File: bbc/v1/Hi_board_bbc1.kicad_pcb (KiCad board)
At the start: 2 copper layers, 55 x 61.1 mm, 15 parts, among them J1 sw-latch, J2 led-latch, J3 GLVMP, SW1 BSPD_RESET, SW2 IMD_RESET, SW3 BMS_RESET

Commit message: Add files via upload
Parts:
- moved J3 7.64 mm to (141.2, 112.3)
- moved J2 7.20 mm to (130.7, 108.5)
- moved R6 6.91 mm to (161.0, 122.4)
- moved R1 6.76 mm to (120.6, 122.4)
- moved J1 6.69 mm to (157.5, 108.4)
- moved D3 6.37 mm to (154.4, 127.5)
- moved D1 6.25 mm to (124.7, 127.5)
- moved R5 5.95 mm to (150.4, 132.6)
- moved R2 5.86 mm to (131.3, 132.6)
- moved R3 5.68 mm to (135.6, 122.4)
- moved R4 5.68 mm to (146.3, 132.6)
- moved D2 5.59 mm to (139.7, 127.5)
- moved SW3 3.24 mm to (153.7, 146.5)
- moved SW1 3.10 mm to (123.7, 146.0)
- moved SW2 2.22 mm to (138.5, 146.0)
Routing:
- net +12V: track 111.4 -> 86.3 mm
- net 0: track 86.6 -> 76.6 mm
- net BMS_RESET: track 52.3 -> 45.7 mm
- net BMS_LED: track 51.0 -> 44.6 mm
- net IMD_LED: track 42.3 -> 38.5 mm
- net BSPD_RESET: track 80.6 -> 76.9 mm
- net IMD_RESET: track 50.3 -> 48.0 mm
- net Net-(R5-Pad1): track 12.7 -> 10.7 mm
- net Net-(R3-Pad1): track 12.7 -> 10.7 mm
- net BSPD_LED: track 22.3 -> 20.3 mm
- net Net-(D3-A): track 11.1 -> 9.58 mm
- net Net-(D1-A): track 10.1 -> 9.16 mm
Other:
- board size 55 x 61.1 mm -> 47.8 x 50.3 mm

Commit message: Add files via upload
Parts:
- moved SW3 0.72 mm to (153.2, 146.0)
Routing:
- net BMS_RESET: track 45.7 -> 44.4 mm
- net +12V: track 86.3 -> 86.9 mm
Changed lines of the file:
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@@
 	(footprint "Button_Switch_THT:SW_PUSH_6mm"
 		(layer "F.Cu")
-		(at 153.706 146.506 90)
+		(at 153.198 145.998 90)
 		(descr "Generic 6mm SW tactile push button")
 		(tags "tact sw push 6mm")
@@
 			(keep_text_aligned yes)
 		)
-		(gr_text "1.36"
+		(gr_text "34.544"
 			(at 178.174 118.872 90)
 			(layer "Cmts.User")
@@
 			(keep_text_aligned yes)
 		)
-		(gr_text "0.755"
+		(gr_text "19.178"
 			(at 166.998 111.189 90)
 			(layer "Cmts.User")
@@
 			(keep_text_aligned yes)
 		)
-		(gr_text "1.16"
+		(gr_text "29.464"
 			(at 140.716 99.434 0)
 			(layer "Cmts.User")
@@
 		(layer "Cmts.User")
 		(pts
+			(xy 140.716 142.748) (xy 155.448 142.748)
+		)
+		(height 13.252)
+		(orientation 0)
+		(format
+			(prefix "")
+			(suffix "")
+			(units 3)
+			(units_format 0)
+			(precision 4)
+			(suppress_zeroes yes)
+		)
+		(style
+			(thickness 0.1)
+			(arrow_length 1.27)
+			(text_position_mode 0)
+			(arrow_direction outward)
+			(extension_height 0.58642)
+			(extension_offset 0.5)
+			(keep_text_aligned yes)
+		)
+		(gr_text "14.732"
+			(at 148.082 154.85 0)
+			(layer "Cmts.User")
+			(effects
+				(font
+					(size 1 1)
+					(thickness 0.15)
+				)
+			)
+		)
+	)
+	(dimension
+		(type orthogonal)
+		(layer "Cmts.User")
+		(pts
 			(xy 155.448 120.778) (xy 164.592 104.14)
 		)
@@
 			(keep_text_aligned yes)
 		)
-		(gr_text "0.36"
+		(gr_text "9.144"
 			(at 160.02 99.434 0)
 			(layer "Cmts.User")
@@
 			(keep_text_aligned yes)
 		)
-		(gr_text "1.88"
+		(gr_text "47.752"
 			(at 140.716 92.322 0)
 			(layer "Cmts.User")
@@
 		)
 	)
+	(dimension
+		(type orthogonal)
+		(layer "Cmts.User")
+		(pts
+			(xy 125.984 142.748) (xy 140.716 142.748)
+		)
+		(height 13.252)
+		(orientation 0)
+		(format
+			(prefix "")
+			(suffix "")
+			(units 3)
+			(units_format 0)
+			(precision 4)
+			(suppress_zeroes yes)
+		)
+		(style
+			(thickness 0.1)
+			(arrow_length 1.27)
+			(text_position_mode 0)
+			(arrow_direction outward)
+			(extension_height 0.58642)
+			(extension_offset 0.5)
+			(keep_text_aligned yes)
+		)
+		(gr_text "14.732"
+			(at 133.35 154.85 0)
+			(layer "Cmts.User")
+			(effects
+				(font
+					(size 1 1)
+					(thickness 0.15)
+				)
+			)
+		)
+	)
 	(segment
 		(start 127.249 128.275)
@@
 	)
 	(segment
-		(start 158.076 146.506)
-		(end 158.206 146.506)
+		(start 125.476 135.128)
+		(end 125.476 138.176)
 		(width 0.8)
-		(layer "F.Cu")
+		(layer "B.Cu")
 		(net 9)
 	)
 	(segment
-		(start 125.476 135.128)
-		(end 125.476 138.176)
+		(start 157.698 145.998)
+		(end 157.698 139.498)
 		(width 0.8)
 		(layer "B.Cu")
@@
 	)
 	(segment
-		(start 125.476 138.176)
-		(end 126.798 139.498)
+		(start 128.234 145.998)
+		(end 131.588 149.352)
 		(width 0.8)
 		(layer "B.Cu")
@@
 	)
 	(segment
-		(start 118.364 111.76)
-		(end 118.364 132.588)
+		(start 125.476 138.176)
+		(end 126.798 139.498)
 		(width 0.8)
 		(layer "B.Cu")
@@
 	)
 	(segment
-		(start 126.798 139.498)
-		(end 128.234 139.498)
+		(start 131.588 149.352)
+		(end 156.148 149.352)
 		(width 0.8)
 		(layer "B.Cu")
@@
 	)
 	(segment
-		(start 119.888 134.112)
-		(end 124.46 134.112)
+		(start 118.364 111.76)
+		(end 118.364 132.588)
 		(width 0.8)
 		(layer "B.Cu")
@@
 	)
 	(segment
-		(start 155.36 149.352)
-		(end 131.588 149.352)
+		(start 126.798 139.498)
+		(end 128.234 139.498)
 		(width 0.8)
 		(layer "B.Cu")
@@
 	)
 	(segment
-		(start 158.206 140.006)
-		(end 158.206 146.506)
+		(start 119.888 134.112)
+		(end 124.46 134.112)
 		(width 0.8)
 		(layer "B.Cu")
@@
 	)
 	(segment
-		(start 158.206 146.506)
-		(end 155.36 149.352)
+		(start 157.698 147.802)
+		(end 157.698 145.998)
 		(width 0.8)
 		(layer "B.Cu")
@@
 	)
 	(segment
-		(start 131.588 149.352)
-		(end 128.234 145.998)
+		(start 124.46 134.112)
+		(end 125.476 135.128)
 		(width 0.8)
 		(layer "B.Cu")
@@
 	)
 	(segment
-		(start 124.46 134.112)
-		(end 125.476 135.128)
+		(start 156.148 149.352)
+		(end 157.698 147.802)
 		(width 0.8)
 		(layer "B.Cu")
@@
 	)
 	(segment
-		(start 152.4 135.128)
-		(end 153.416 134.112)
+		(start 153.198 139.498)
+		(end 153.198 145.998)
 		(width 0.8)
 		(layer "B.Cu")
@@
 	)
 	(segment
-		(start 153.706 140.006)
-		(end 153.706 146.506)
+		(start 152.4 138.7)
+		(end 153.198 139.498)
 		(width 0.8)
 		(layer "B.Cu")
@@
 	)
 	(segment
-		(start 153.416 134.112)
-		(end 161.493314 134.112)
-		(width 0.8)
-		(layer "B.Cu")
-		(net 11)
-	)
-	(segment
-		(start 162.56 117.348)
-		(end 159.126 113.914)
+		(start 152.4 135.128)
+		(end 153.416 134.112)
 		(width 0.8)
 		(layer "B.Cu")
@@
 	)
 	(segment
-		(start 152.4 139.7)
-		(end 152.4 135.128)
+		(start 152.4 135.128)
+		(end 152.4 138.7)
 		(width 0.8)
 		(layer "B.Cu")
@@
 	)
 	(segment
-		(start 152.706 140.006)
-		(end 152.4 139.7)
+		(start 153.416 134.112)
+		(end 161.493314 134.112)
 		(width 0.8)
 		(layer "B.Cu")
@@
 	)
 	(segment
-		(start 153.706 140.006)
-		(end 152.706 140.006)
+		(start 162.56 117.348)
+		(end 159.126 113.914)
 		(width 0.8)
 		(layer "B.Cu")
@@
 	)
 	(segment
+		(start 152.908 143.256)
+		(end 150.166 145.998)
+		(width 0.8)
+		(layer "F.Cu")
+		(net 12)
+	)
+	(segment
 		(start 158.496 119.888)
 		(end 155.448 116.84)
@@
 	)
 	(segment
-		(start 152.908 143.256)
-		(end 161.036 143.256)
+		(start 161.036 143.256)
+		(end 152.908 143.256)
 		(width 0.8)
 		(layer "F.Cu")
@@
 	)
 	(segment
-		(start 150.166 145.998)
-		(end 152.908 143.256)
-		(width 0.8)
-		(layer "F.Cu")
-		(net 12)
-	)
-	(segment
 		(start 161.036 143.256)
 		(end 163.068 141.224)
@@
 	)
 	(segment
-		(start 152.4 137.668)
-		(end 150.876 139.192)
+		(start 138.466 145.998)
+		(end 141.716 142.748)
 		(width 0.8)
 		(layer "F.Cu")
@@
 	)
 	(segment
-		(start 138.466 145.998)
-		(end 141.716 142.748)
+		(start 145.288 142.748)
+		(end 148.844 139.192)
 		(width 0.8)
 		(layer "F.Cu")
@@
 	)
 	(segment
-		(start 145.288 142.748)
-		(end 148.844 139.192)
+		(start 152.4 137.668)
+		(end 150.876 139.192)
 		(width 0.8)
 		(layer "F.Cu")

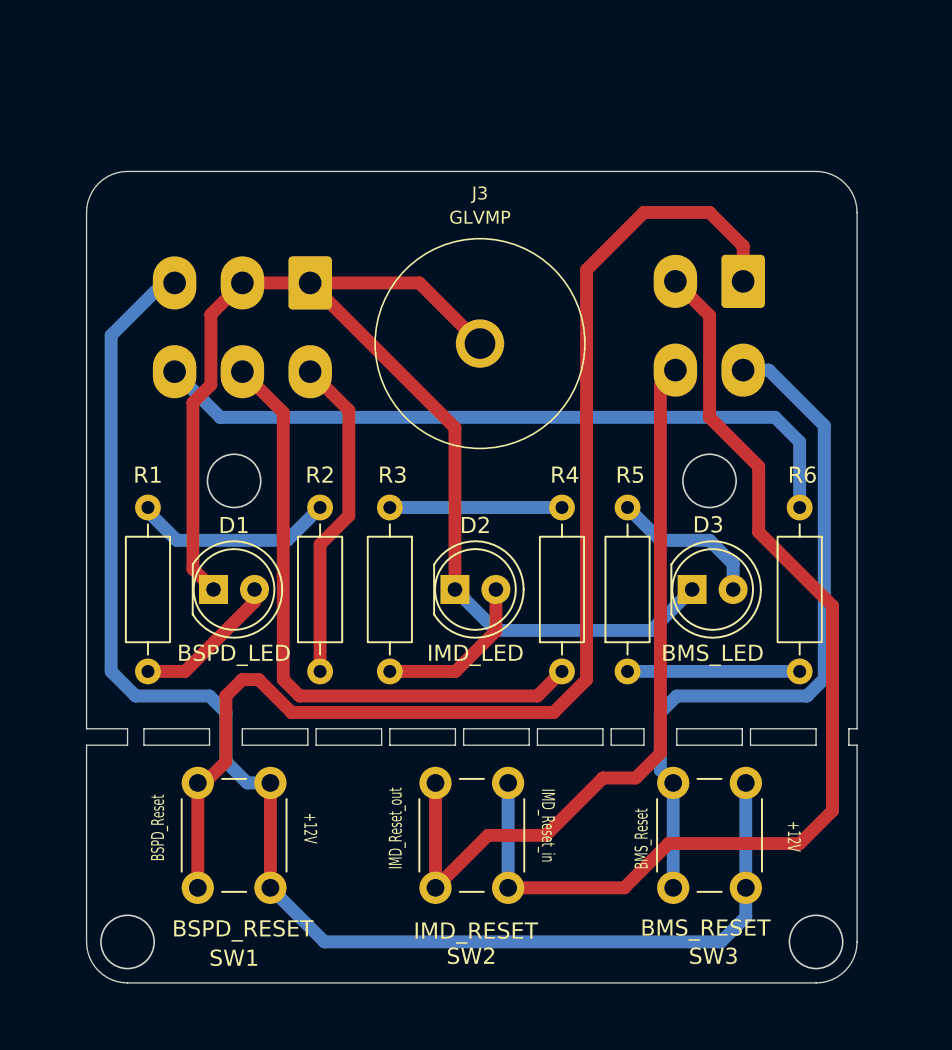
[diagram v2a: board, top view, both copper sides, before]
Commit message: swapped BBC ports
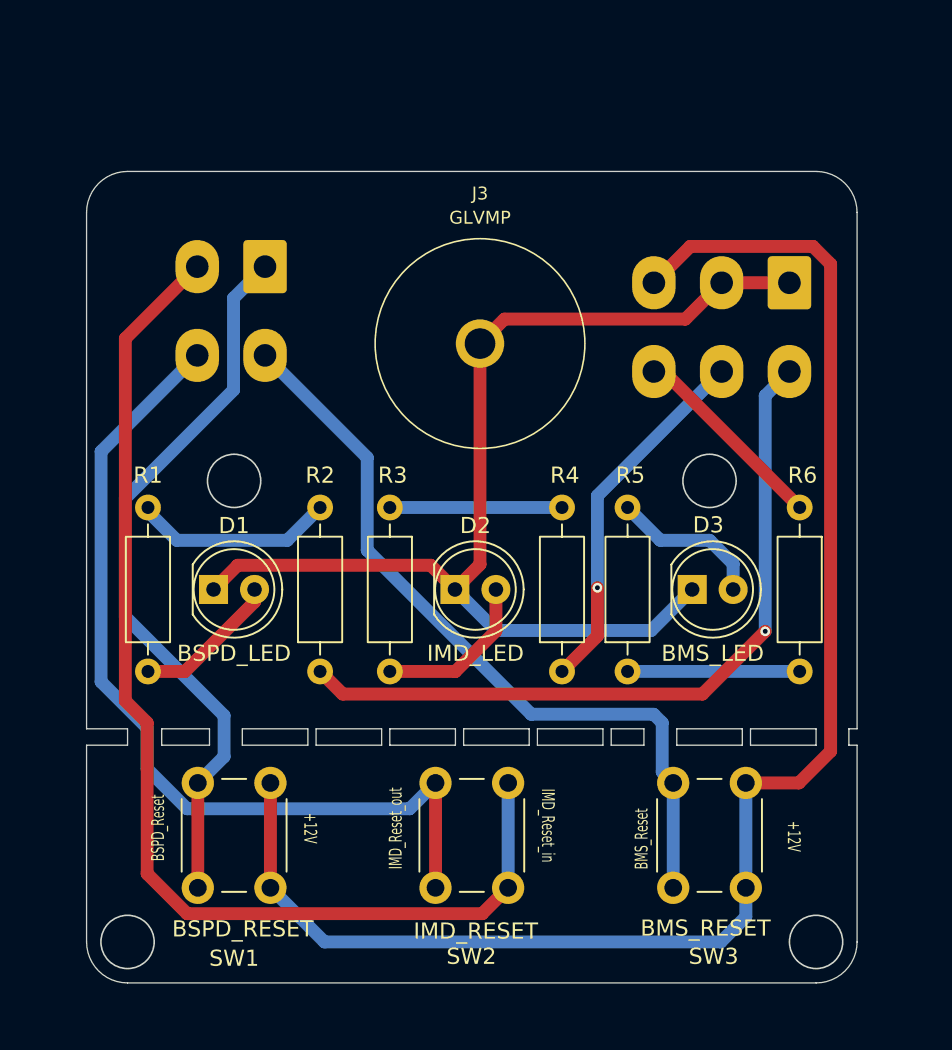
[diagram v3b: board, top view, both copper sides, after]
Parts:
- moved J2 29.7 mm to (160.4, 108.5)
- moved J1 29.6 mm to (127.9, 107.5)
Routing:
- net BMS_LED: track 44.6 -> 12.5 mm
- net BSPD_RESET: track 76.9 -> 45.3 mm
- net BSPD_LED: track 20.3 -> 46.5 mm, vias 0 -> 1
- net IMD_LED: track 38.5 -> 22.7 mm, vias 0 -> 1
- net +12V: track 86.9 -> 94.9 mm
- net IMD_RESET: track 48.0 -> 55.3 mm
- net 0: track 76.6 -> 69.6 mm
- net Net-(J1-Pin_2): track 65.4 -> 70.6 mm
- net BMS_RESET: track 44.4 -> 47.9 mm
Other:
- outline, holes or cut-outs redrawn
